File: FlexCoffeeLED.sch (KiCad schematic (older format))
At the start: 8 parts

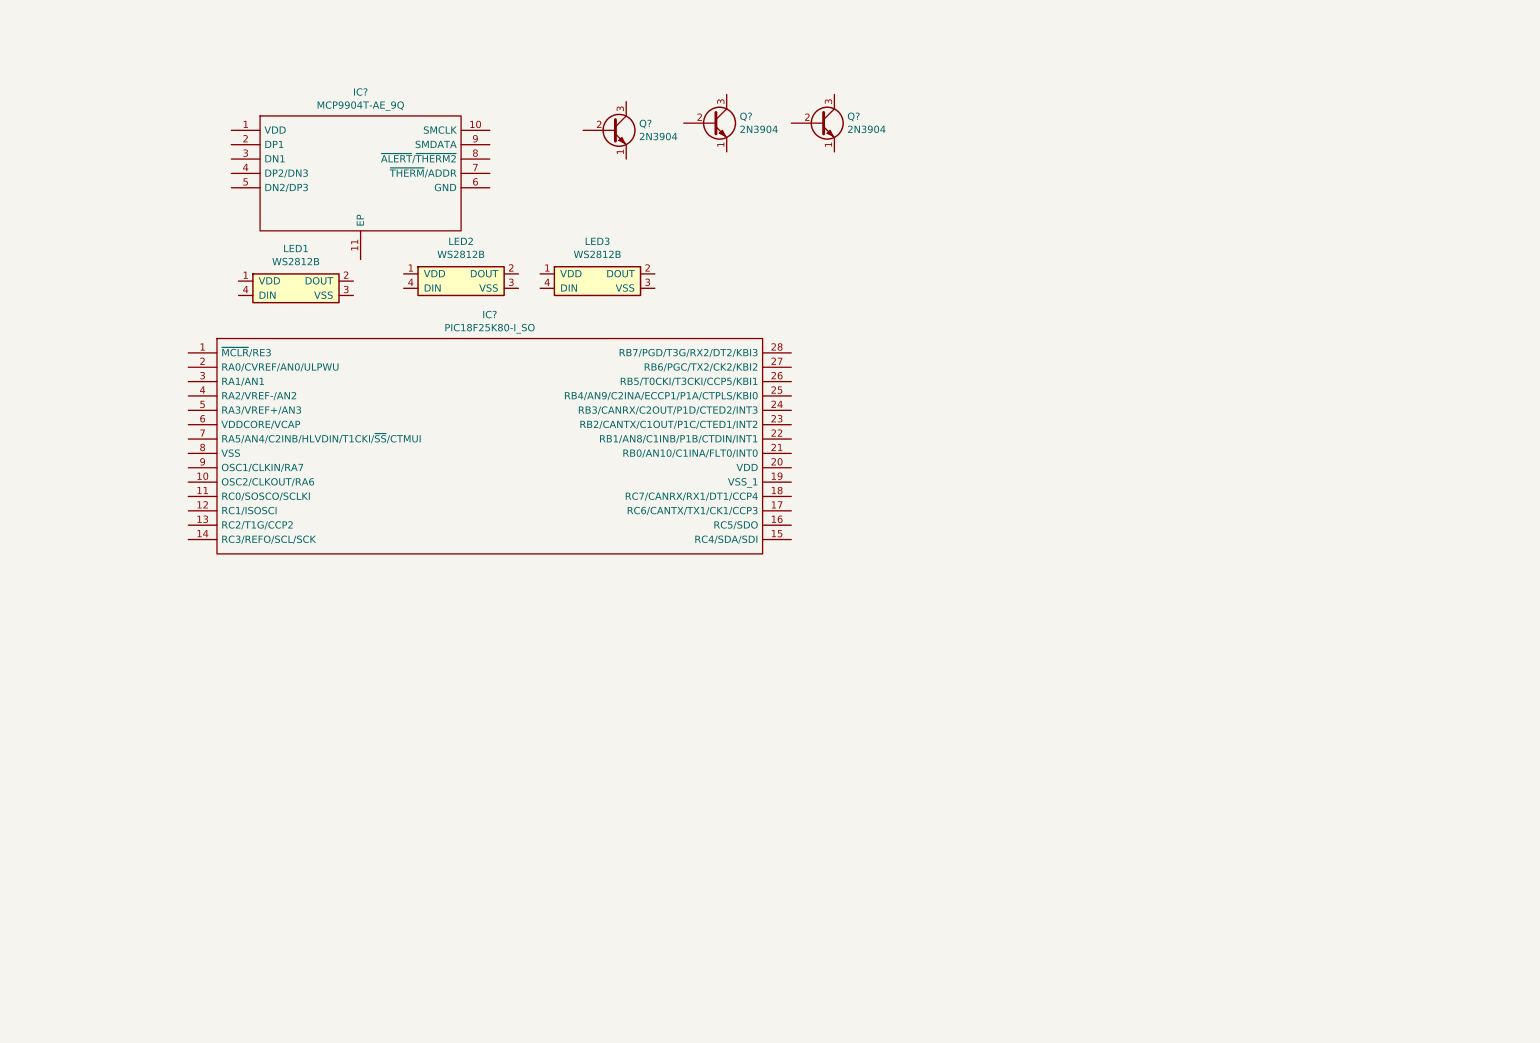
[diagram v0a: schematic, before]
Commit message: Added Data Sheets Drew Wires and added passive components and connectors
Changes Committed:
	new file:   Datasheet/MCP990_234.pdf
	new file:   Datasheet/MCP990_234_AN10.14.pdf
	new file:   Datasheet/MCP990_234_AN12.14.pdf
	new file:   Datasheet/NCP718-D-1315705.pdf
	new file:   Datasheet/Pic18F66k80.pdf
	new file:   Datasheet/PicKit3_Poster.pdf
	new file:   Datasheet/PicKit3_UserGuide.pdf
	new file:   Datasheet/WS2812B.pdf
	modified:   FlexCoffeeLED-cache.lib
	modified:   FlexCoffeeLED.bak
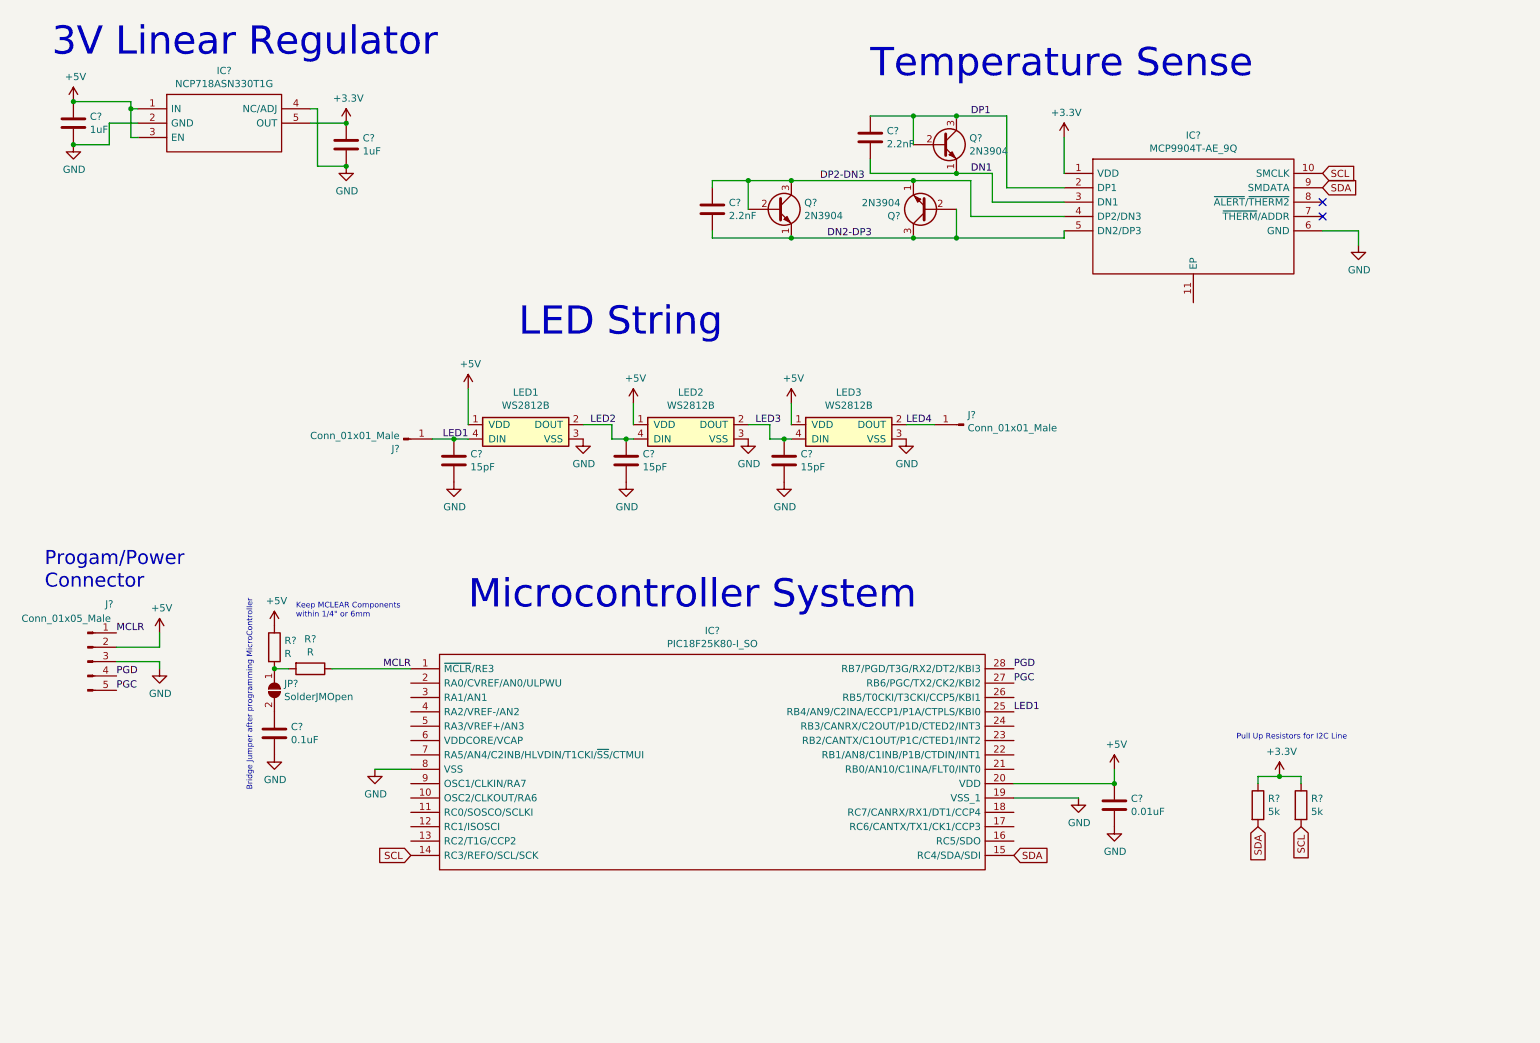
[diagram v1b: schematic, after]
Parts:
- added C? (x2): 1uF, symbol device:C
- added C? (x3): 15pF, symbol device:C
- added C?: 0.01uF, symbol device:C
- added C?: 0.1uF, symbol device:C
- added C? (x2): 2.2nF, symbol device:C
- added IC?: NCP718ASN330T1G, SOT95P280X100-5N, symbol SamacSys_Parts:NCP718ASN330T1G
- added J?: Conn_01x05_Male, symbol Connector:Conn_01x05_Male
- added J? (x2): Conn_01x01_Male, symbol Connector:Conn_01x01_Male
- added JP?: SolderJMOpen, symbol Jumper:SolderJumper_2_Open
- added R? (x2): 5k, symbol device:R
- added R? (x2): R, symbol device:R
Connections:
- net +5V: now reaches LED1.1 (VDD)
- net +5V: now also IC?.20 (VDD), LED2.1 (VDD), LED3.1 (VDD), C?.1, C?.1, IC?.1 (IN), IC?.3 (EN), J?.2 (Pin_2), R?.1
- net LED2: now reaches LED1.2 (DOUT)
- net LED2: now also LED2.4 (DIN), C?.1
- net GND: now reaches LED1.3 (VSS)
- net GND: now also IC?.19 (VSS_1), IC?.6 (GND), IC?.8 (VSS), LED2.3 (VSS), LED3.3 (VSS), C?.2, C?.2, C?.2, C?.2, C?.2, C?.2, C?.2, IC?.2 (GND), IC?.4 (NC/ADJ), J?.3 (Pin_3)
- net LED1: now reaches LED1.4 (DIN)
- net LED1: now also IC?.25 (RB4/AN9/C2INA/ECCP1/P1A/CTPLS/KBI0), C?.1, J?.1 (Pin_1)
- net LED3: now reaches LED2.2 (DOUT)
- net LED3: now also LED3.4 (DIN), C?.1
- net LED4: now reaches LED3.2 (DOUT)
- net LED4: now also J?.1 (Pin_1)
- net +3V3: now reaches IC?.1 (VDD)
- net +3V3: now also C?.1, IC?.5 (OUT), R?.1, R?.1
- net SCL: now reaches IC?.10 (SMCLK)
- net SCL: now also IC?.14 (RC3/REFO/SCL/SCK), R?.2
- net DP1: now reaches IC?.2 (DP1)
- net DP1: now also Q?.2 (B), Q?.3 (C), C?.1
- net DN1: now reaches IC?.3 (DN1)
- net DN1: now also Q?.1 (E), C?.2
- net DP2-DN3: now reaches IC?.4 (DP2/DN3)
- net DP2-DN3: now also Q?.1 (E), Q?.2 (B), Q?.3 (C), C?.1
- net DN2-DP3: now reaches IC?.5 (DN2/DP3)
- net DN2-DP3: now also Q?.1 (E), Q?.2 (B), Q?.3 (C), C?.2
- net SDA: now reaches IC?.9 (SMDATA)
- net SDA: now also IC?.15 (RC4/SDA/SDI), R?.2
- net MCLR: now reaches IC?.1 (~MCLR~/RE3)
- net MCLR: now also J?.1 (Pin_1), R?.1
- net PGC: now reaches IC?.27 (RB6/PGC/TX2/CK2/KBI2)
- net PGC: now also J?.5 (Pin_5)
- net PGD: now reaches IC?.28 (RB7/PGD/T3G/RX2/DT2/KBI3)
- net PGD: now also J?.4 (Pin_4)
- new net: JP?.1 (A), R?.2, R?.2
- new net: C?.1, JP?.2 (B)
- no-connect marks 0 -> 2
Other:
- note added: "3V Linear Regulator"
- note added: "Bridge Jumper after programming MicroController"
- note added: "Keep MCLEAR Components \nwithin 1/4" or 6mm"
- note added: "LED String"
- note added: "Microcontroller System"
- note added: "Progam/Power\nConnector\n"
- note added: "Pull Up Resistors for I2C Line\n"
- note added: "Temperature Sense"
- moved on the sheet: IC?, LED1, LED2, LED3, Q?

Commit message: Added Voltage Translator to I2C
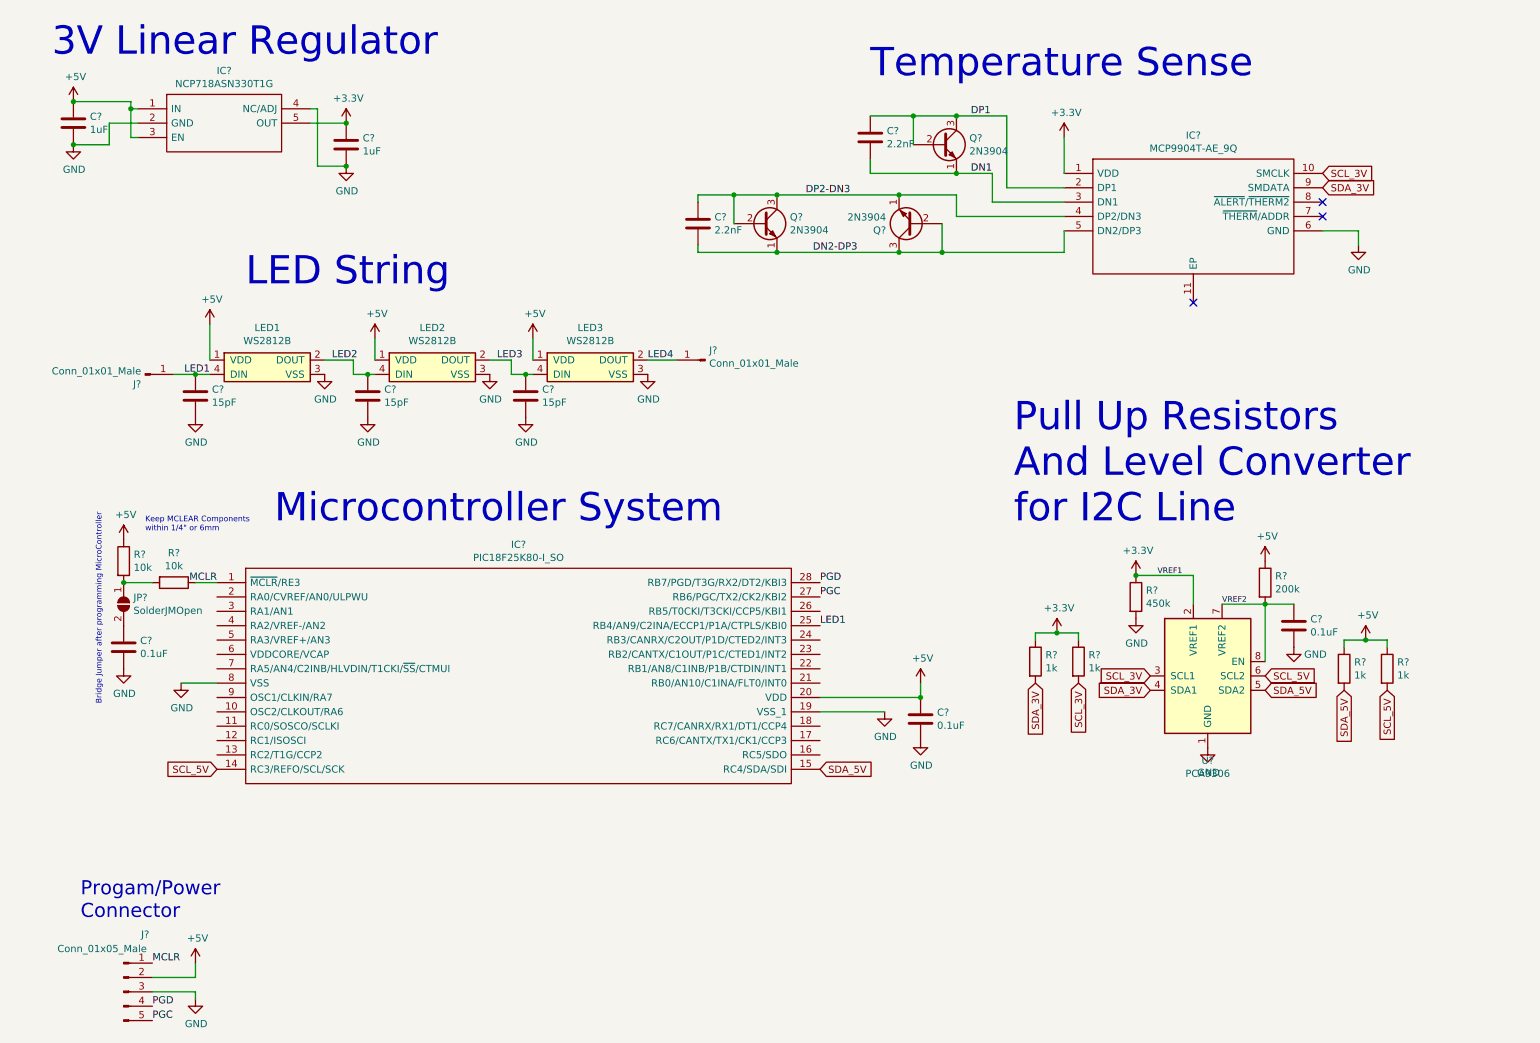
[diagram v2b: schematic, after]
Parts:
- added C?: 0.1uF, symbol device:C
- added R? (x2): 1k, symbol device:R
- added R?: 450k, symbol device:R
- added R?: 200k, symbol device:R
- added U?: PCA9306, symbol interface:PCA9306
- C?: value 0.01uF -> 0.1uF
- R? (x2): value 5k -> 1k
- R? (x2): value R -> 10k
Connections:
- net +3V3: now also R?.1, U?.2 (VREF1)
- net +5V: now also R?.1, R?.1, R?.1
- net GND: now also C?.2, R?.2, U?.1 (GND)
- net SCL renamed SCL_3V
- net SCL_3V: now also U?.3 (SCL1); no longer IC?.14 (RC3/REFO/SCL/SCK)
- net SDA renamed SDA_3V
- net SDA_3V: now also U?.4 (SDA1); no longer IC?.15 (RC4/SDA/SDI)
- new net SCL_5V: IC?.14 (RC3/REFO/SCL/SCK), R?.2, U?.6 (SCL2)
- new net SDA_5V: IC?.15 (RC4/SDA/SDI), R?.2, U?.5 (SDA2)
- new net VREF2: C?.1, R?.2, U?.7 (VREF2), U?.8 (EN)
- no-connect marks 2 -> 3
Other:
- note added: "Pull Up Resistors \nAnd Level Converter\nfor I2C Line"
- note removed: "Pull Up Resistors for I2C Line\n"
- moved on the sheet: C?, IC?, J?, JP?, LED1, LED2, LED3, Q?, R?

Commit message: added no connects to up
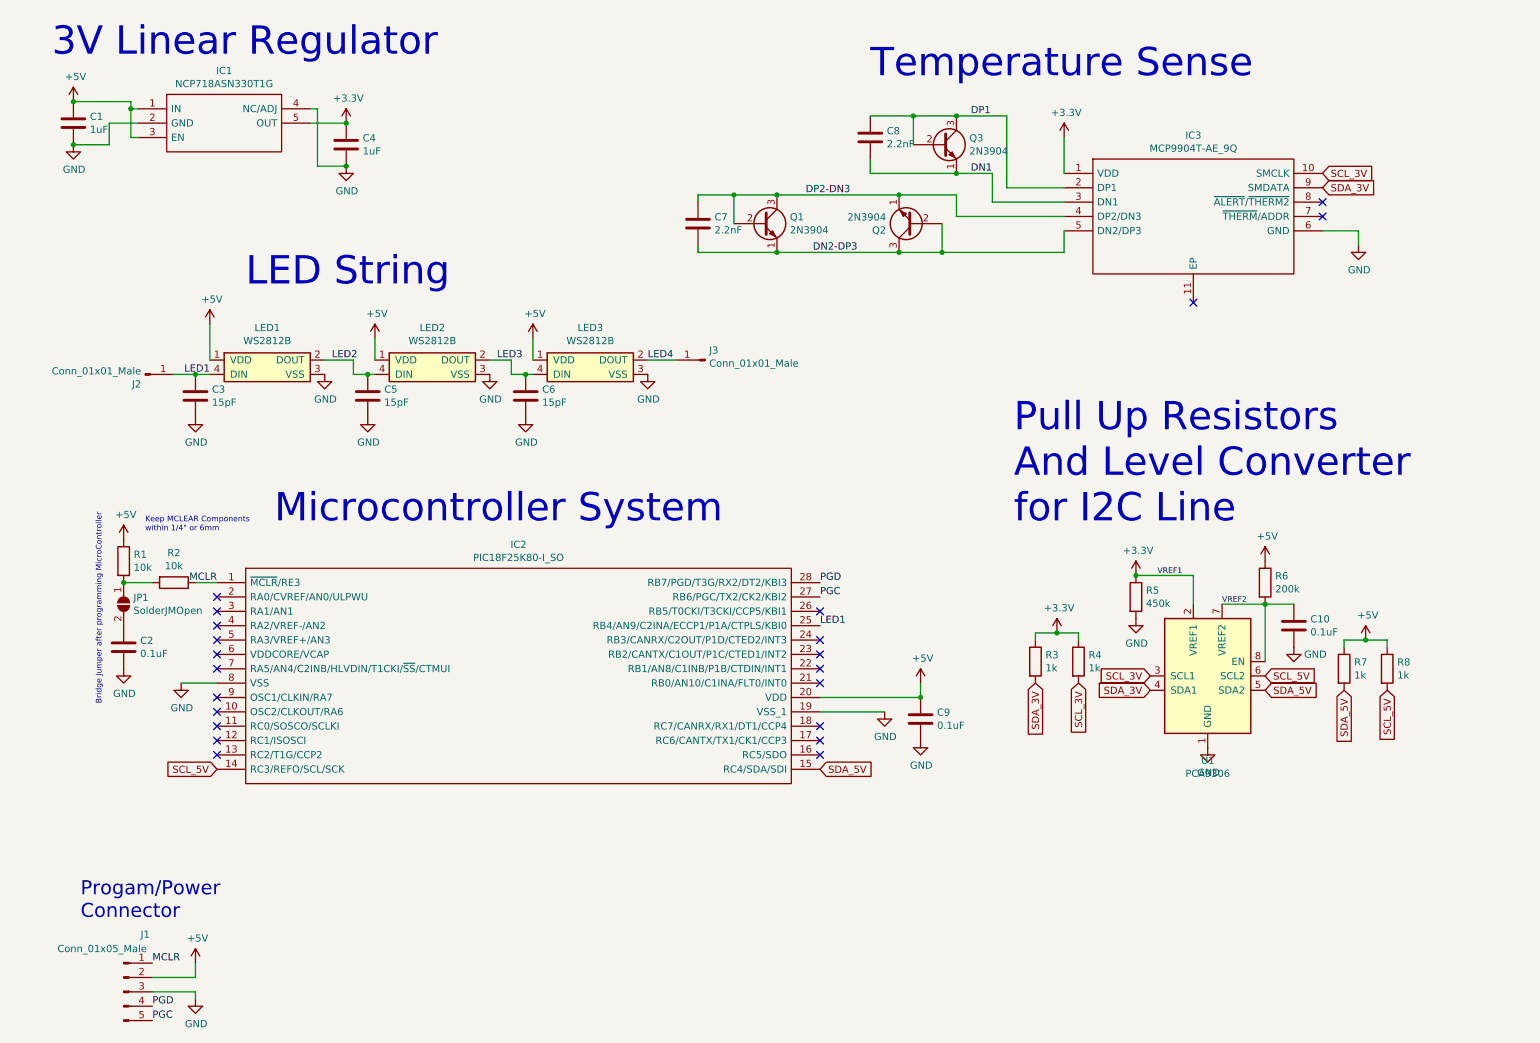
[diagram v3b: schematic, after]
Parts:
- gave numbers to parts that had none: 29
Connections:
- no-connect marks 3 -> 22
